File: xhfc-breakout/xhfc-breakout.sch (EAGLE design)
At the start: 78 parts, among them Q1 BC848CSMD, Q2 BC848CSMD, Q3 BC848CSMD, Q4 BC848CSMD, U1 XHFC-2SU, X1 UEXT

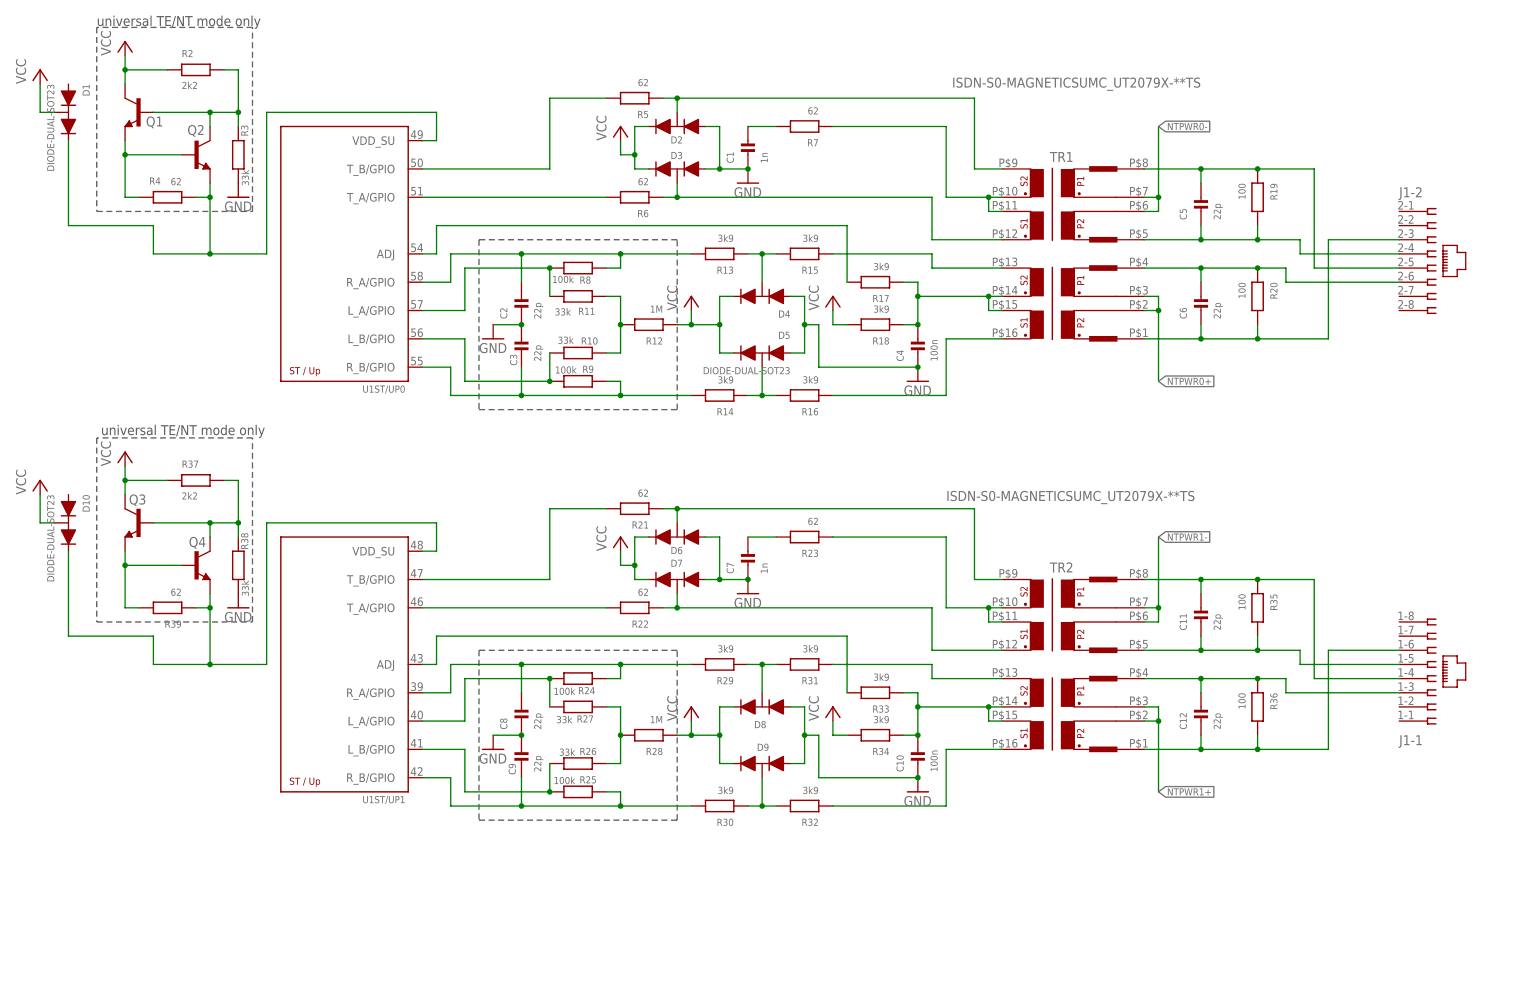
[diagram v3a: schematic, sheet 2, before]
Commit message: xhfc-breakout: more WIP layout + schematics work
schematics should be done now, layout about 65%
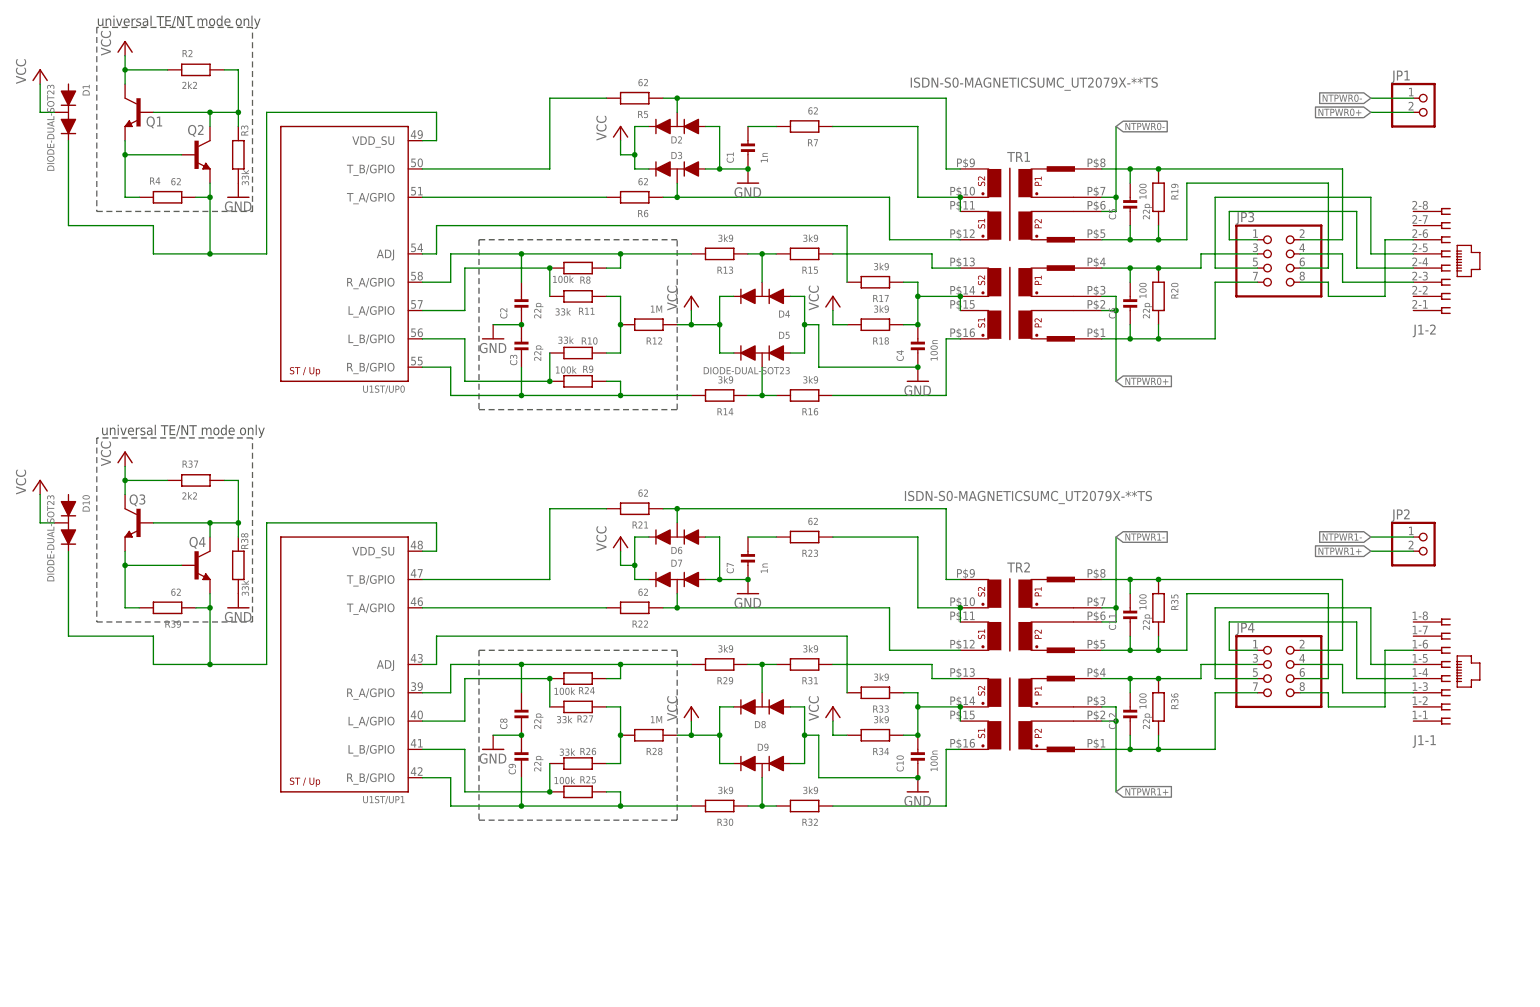
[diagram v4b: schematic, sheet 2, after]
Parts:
- added C21, C22: 10n, rc-sysmocom:CAP_CERAMIC_0603
- added JP1, JP2: (no value), laforge:PINHD-1X2
- added JP3, JP4: (no value), pinhead:PINHD-2X4
- added Q5: (no value), tcxo:VCXO-EN-VKB
- added R40, R42: 47, rc-sysmocom:RESISTOR_0603
- added R41: 1k5, rc-sysmocom:RESISTOR_0603
- C20: value 33n -> 10n
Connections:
- new net CLK_OUT: R42.2
- new net N$50: C6.2, JP3.3, R20.1, TR1.4
- new net N$52: J1-2.3, JP3.4
- new net N$53: J1-2.6, JP3.8
- new net N$54: J1-1.4, JP4.1
- new net N$55: J1-1.5, JP4.5
- new net N$56: J1-1.3, JP4.4
- new net N$61: J1-1.6, JP4.8
- new net N$62: C21.2, Q5.ADJ, R41.1
- new net N$63: R42.1, U1CLOCK.CLK_OUT/GPIO7
- new net N$64: Q5.OUT, R40.1
- new net N$8: J1-2.4, JP3.1
- new net VCXO_OUT: R40.2, U1CLOCK.OSC_IN
- new net VCXO_VCTRL: C22.2, R41.2
- net !INT: now also X1.RXD
- net !RES: now also X1.TXD
- net GND: now also C21.1, C22.1, Q5.GND, U1CLOCK.WAKEUP/WD
- net N$18: now also JP3.2; no longer J1-2.5
- net N$21: now also JP3.6; no longer J1-2.4
- net N$25: now also J1-2.5, JP3.5; no longer C6.2, J1-2.6, R20.1, TR1.4
- net N$26: now also JP3.7; no longer J1-2.3
- net N$43: now also JP4.2; no longer J1-1.4
- net N$44: now also JP4.6; no longer J1-1.5
- net N$45: now also JP4.3; no longer J1-1.3
- net N$46: now also JP4.7; no longer J1-1.6
- net NTPWR0+: now also JP1.2
- net NTPWR0-: now also JP1.1
- net NTPWR1+: now also JP2.2
- net NTPWR1-: now also JP2.1
- net VCC: now also Q5.EN, Q5.VDD
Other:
- moved on the sheet: C11, C12, C20, C5, C6, J1-1, J1-2, R19, R20, R35, R36, TR1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

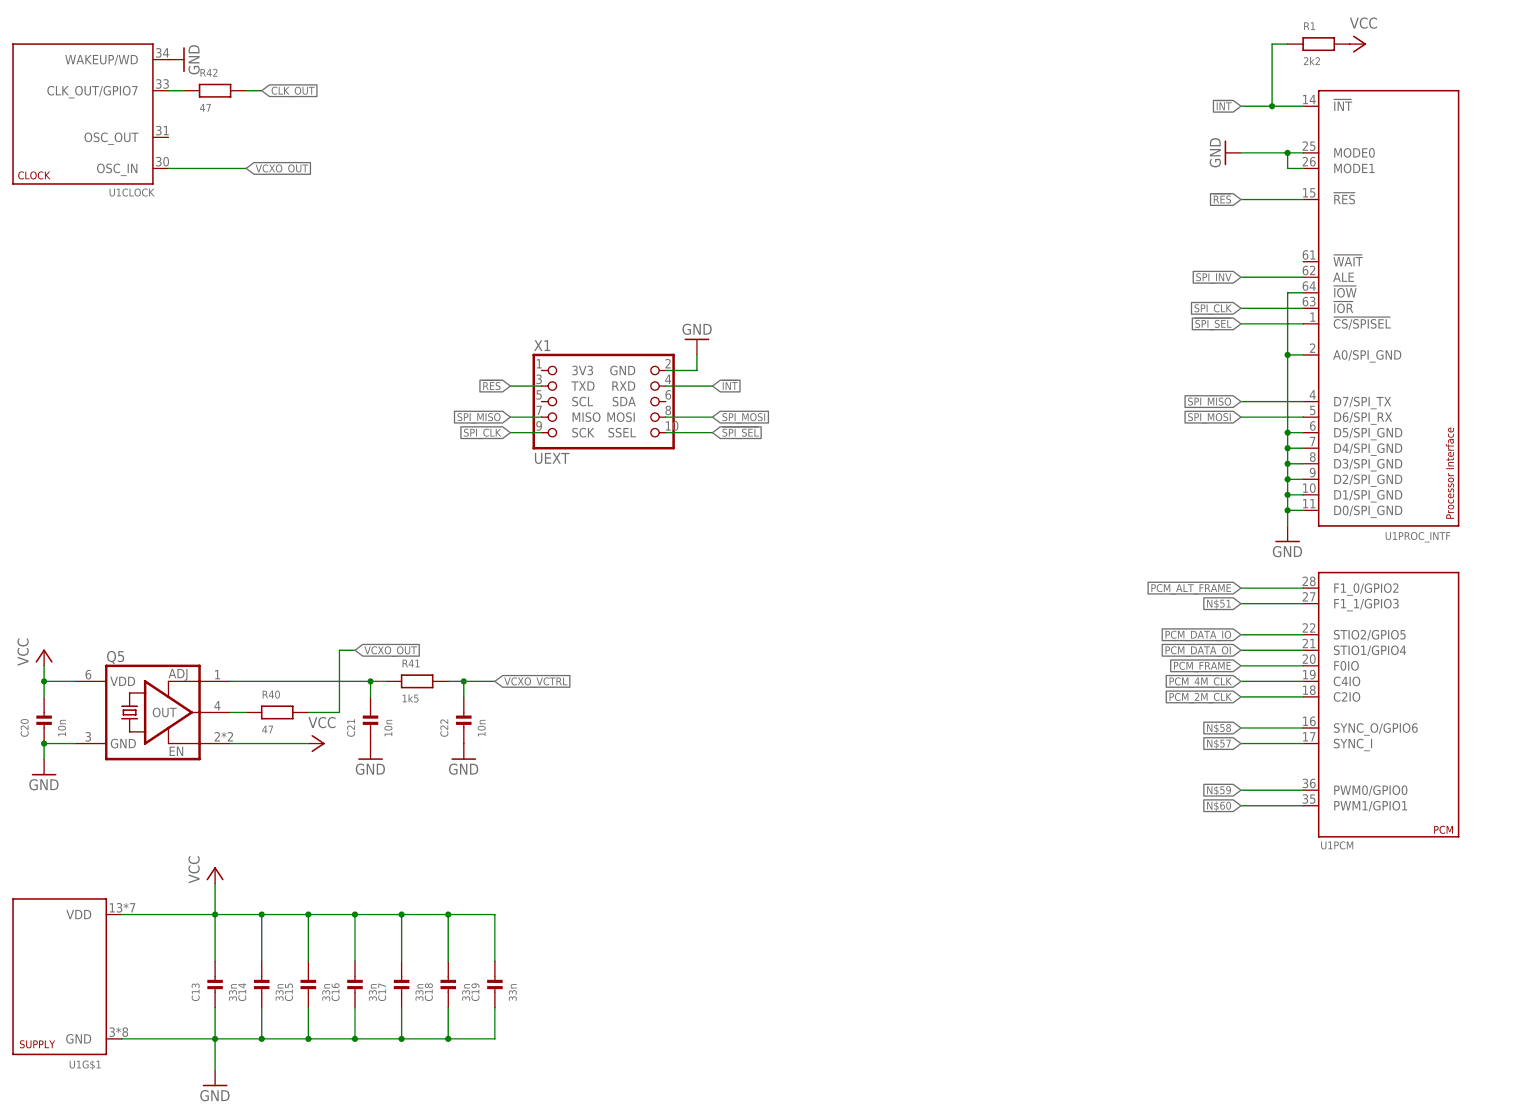
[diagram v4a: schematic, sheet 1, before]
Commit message: xhfc-breakout: Complete routing of v1 board
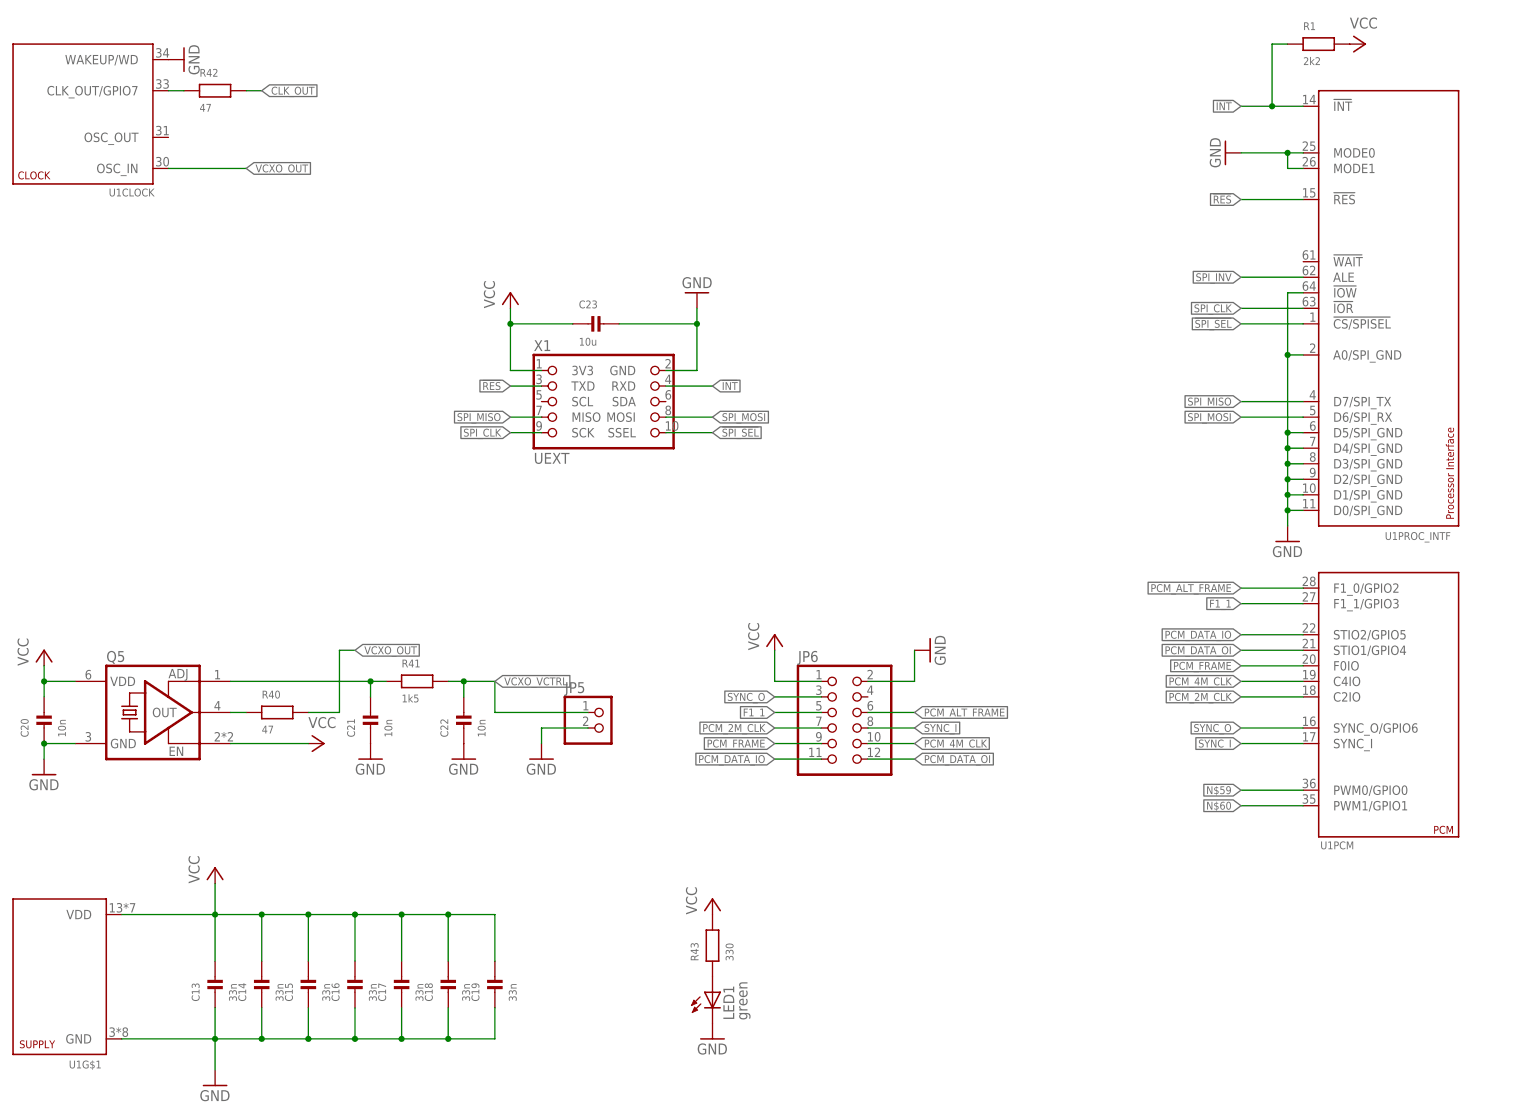
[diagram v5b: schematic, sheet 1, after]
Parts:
- added C23: 10u, rc-sysmocom:CAP_CERAMIC1206
- added JP5: (no value), laforge:PINHD-1X2
- added JP6: (no value), pinhead:PINHD-2X6
- added LED1: green, led:LEDCHIP-LED0603
- added R43: 330, rc-sysmocom:RESISTOR_0603
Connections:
- net N$11 renamed P0_R_B
- net N$12 renamed P0_R_A
- net N$13 renamed P0_L_A
- net N$14 renamed P0_ADJ
- net N$15 renamed P0_L_B
- net N$2 renamed P0_T_B
- net N$28 renamed P1_T_B
- net N$29 renamed P1_T_A
- net N$32 renamed P1_ADJ
- net N$33 renamed P1_R_B
- net N$34 renamed P1_R_A
- net N$35 renamed P1_L_A
- net N$36 renamed P1_L_B
- net N$4 renamed P0_VDD_SU
- net N$49 renamed P1_VDD_SU
- net N$5 renamed P0_T_A
- removed net N$51: U1PCM.F1_1/GPIO3
- removed net N$57: U1PCM.SYNC_I
- removed net N$58: U1PCM.SYNC_O/GPIO6
- new net F1_1: JP6.5, U1PCM.F1_1/GPIO3
- new net N$2: LED1.A, R43.1
- new net SYNC_I: JP6.8, U1PCM.SYNC_I
- new net SYNC_O: JP6.3, U1PCM.SYNC_O/GPIO6
- net GND: now also C23.2, JP5.2, JP6.2, LED1.C
- net PCM_2M_CLK: now also JP6.7
- net PCM_4M_CLK: now also JP6.10
- net PCM_ALT_FRAME: now also JP6.6
- net PCM_DATA_IO: now also JP6.11
- net PCM_DATA_OI: now also JP6.12
- net PCM_FRAME: now also JP6.9
- net VCC: now also C23.1, JP6.1, R43.2, X1.3V3
- net VCXO_VCTRL: now also JP5.1

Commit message: xhfc-breakout: bom attributes
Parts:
- C1, C10, C11, C12, C13, C14, C15, C16, C17, C18, C19, C2, C20, C21, C22, C23, C3, C4, C5, C6, C7, C8, C9: CLASS (none) -> CAPACITOR; DESCRIPTION (none) -> NO DESCRIPTION; LINK (none) -> UNKNOWN LINK; MANUFACTURER (none) -> UNKNOWN MANUFACTURER; MANUFACTURERPARTNUMBER (none) -> UNKNOWN MANUFACTURER PART NUMBER; POPULATED (none) -> TRUE; ROHSCERTIFICATE (none) -> UNKNOWN ROHS CERTIFICATE; SOURCE (none) -> UNKNOWN SOURCE; SOURCEPARTNUMBER (none) -> UNKNOWN SOURCE PART NUMBER
- D1, D10, D2, D3, D4, D5, D6, D7, D8, D9: CLASS (none) -> DIODE; DATASHEET (none) -> https://assets.nexperia.com/documents/data-sheet/BAV99_SER.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; DESCRIPTION (none) -> DIODE ARRAY GP 100V 150MA SOT323; LINK (none) -> https://www.digikey.com/en/products/detail/nexperia-usa-inc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; MANUFACTURER (none) -> Nexperia USA Inc.; MANUFACTURERPARTNUMBER (none) -> BAV99W,115; POPULATED (none) -> TRUE; ROHSCERTIFICATE (none) -> ROHS3 Compliant; SOURCE (none) -> DIGIKEY; SOURCEPARTNUMBER (none) -> 1727-2915-6-ND
- J1: CLASS (none) -> CONNECTOR\JUMPER; DATASHEET (none) -> https://www.te.com/commerce/DocumentDelivery/DDEController?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; DESCRIPTION (none) -> CONN MOD JACK 8P8C R/A UNSHLD; LINK (none) -> https://www.digikey.com/en/products/detail/te-connectivity-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; MANUFACTURER (none) -> TE Connectivity AMP Connectors; MANUFACTURERPARTNUMBER (none) -> 5557560-1; POPULATED (none) -> TRUE; ROHSCERTIFICATE (none) -> RoHS Compliant; SOURCE (none) -> DIGIKEY; SOURCEPARTNUMBER (none) -> A31449-ND
- JP1, JP2, JP3, JP4, JP5, JP6: CLASS (none) -> CONNECTOR\JUMPER; DESCRIPTION (none) -> NO DESCRIPTION; LINK (none) -> UNKNOWN LINK; MANUFACTURER (none) -> UNKNOWN MANUFACTURER; MANUFACTURERPARTNUMBER (none) -> UNKNOWN MANUFACTURER PART NUMBER; POPULATED (none) -> TRUE; ROHSCERTIFICATE (none) -> UNKNOWN ROHS CERTIFICATE; SOURCE (none) -> UNKNOWN SOURCE; SOURCEPARTNUMBER (none) -> UNKNOWN SOURCE PART NUMBER
- LED1: CLASS (none) -> LED; DESCRIPTION (none) -> NO DESCRIPTION; LINK (none) -> UNKNOWN LINK; MANUFACTURER (none) -> UNKNOWN MANUFACTURER; MANUFACTURERPARTNUMBER (none) -> UNKNOWN MANUFACTURER PART NUMBER; POPULATED (none) -> TRUE; ROHSCERTIFICATE (none) -> UNKNOWN ROHS CERTIFICATE; SOURCE (none) -> UNKNOWN SOURCE; SOURCEPARTNUMBER (none) -> UNKNOWN SOURCE PART NUMBER
- Q1, Q2, Q3, Q4: CLASS (none) -> TRANSISTOR\MOSFET; DATASHEET (none) -> https://www.onsemi.com/pdf/datasheet/bc846awt1-d.pdf; DESCRIPTION (none) -> TRANS NPN 30V 100MA SC70-3; LINK (none) -> https://www.digikey.com/en/products/detail/onsemi/BC848CWT1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; MANUFACTURER (none) -> onsemi; MANUFACTURERPARTNUMBER (none) -> BC848CWT1G; POPULATED (none) -> TRUE; ROHSCERTIFICATE (none) -> ROHS3 Compliant; SOURCE (none) -> DIGIKEY; SOURCEPARTNUMBER (none) -> BC848CWT1GOSDKR-ND
- Q5: CLASS (none) -> TRANSISTOR\MOSFET; DATASHEET (none) -> https://www.conwin.com/datasheets/vx/vx604.pdf; DESCRIPTION (none) -> XTAL OSC VCXO 24.5760MHZ LVCMOS; LINK (none) -> https://www.digikey.com/en/products/detail/connor-winfield/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; MANUFACTURER (none) -> Connor Winfield; MANUFACTURERPARTNUMBER (none) -> VKB51B2-024.576M; POPULATED (none) -> TRUE; ROHSCERTIFICATE (none) -> ROHS3 Compliant; SOURCE (none) -> DIGIKEY; SOURCEPARTNUMBER (none) -> CW967CT-ND
- R1, R10, R11, R12, R13, R14, R15, R16, R17, R18, R19, R2, R20, R21, R22, R23, R24, R25, R26, R27, R28, R29, R3, R30, R31, R32, R33, R34, R35, R36, R37, R38, R39, R4, R40, R41, R42, R43, R5, R6, R7, R8, R9: CLASS (none) -> RESISTOR; DESCRIPTION (none) -> NO DESCRIPTION; LINK (none) -> UNKNOWN LINK; MANUFACTURER (none) -> UNKNOWN MANUFACTURER; MANUFACTURERPARTNUMBER (none) -> UNKNOWN MANUFACTURER PART NUMBER; POPULATED (none) -> TRUE; ROHSCERTIFICATE (none) -> UNKNOWN ROHS CERTIFICATE; SOURCE (none) -> UNKNOWN SOURCE; SOURCEPARTNUMBER (none) -> UNKNOWN SOURCE PART NUMBER
- TR1, TR2: CLASS (none) -> UNKNOWN CLASS; DESCRIPTION (none) -> NO DESCRIPTION; LINK (none) -> UNKNOWN LINK; MANUFACTURER (none) -> UMEC; MANUFACTURERPARTNUMBER (none) -> UT20795-5MTS; POPULATED (none) -> TRUE; ROHSCERTIFICATE (none) -> UNKNOWN ROHS CERTIFICATE; SOURCE (none) -> UMEC; SOURCEPARTNUMBER (none) -> UNKNOWN SOURCE PART NUMBER
- U1: CLASS (none) -> IC; DESCRIPTION (none) -> NO DESCRIPTION; LINK (none) -> UNKNOWN LINK; MANUFACTURER (none) -> UNKNOWN MANUFACTURER; MANUFACTURERPARTNUMBER (none) -> XHFC-2SU; POPULATED (none) -> TRUE; ROHSCERTIFICATE (none) -> UNKNOWN ROHS CERTIFICATE; SOURCE (none) -> CologneChip; SOURCEPARTNUMBER (none) -> UNKNOWN SOURCE PART NUMBER
- X1: CLASS (none) -> CONNECTOR; DESCRIPTION (none) -> NO DESCRIPTION; LINK (none) -> UNKNOWN LINK; MANUFACTURER (none) -> UNKNOWN MANUFACTURER; MANUFACTURERPARTNUMBER (none) -> UNKNOWN MANUFACTURER PART NUMBER; POPULATED (none) -> TRUE; ROHSCERTIFICATE (none) -> UNKNOWN ROHS CERTIFICATE; SOURCE (none) -> UNKNOWN SOURCE; SOURCEPARTNUMBER (none) -> UNKNOWN SOURCE PART NUMBER
